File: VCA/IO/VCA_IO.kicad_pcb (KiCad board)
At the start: 2 copper layers, 29.5 x 111.8 mm, 15 parts, among them J1 Out_B, J10 IO_B, J11 Power, J2 CV1_B, J3 In_B, J4 CV2_B, J5 IO_A, J6 CV1_A, J7 In_A, J8 CV2_A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

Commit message: Clean up VCA boards
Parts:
- added REF**: OSHW-Logo2_7.3x6mm_SilkScreen, Symbol:OSHW-Logo2_7.3x6mm_SilkScreen, B.Cu at (69.8, 64.8)
- J10, J5: moved to B.Cu
- moved J10 0.63 mm to (91.4, 106.7), turned to 180 degrees
- turned J5 to 180 degrees
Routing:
- net Net-(J10-Pad2): track 17.6 -> 19.5 mm
- net Net-(J1-PadT): track 30.3 -> 31.5 mm
- net Net-(J10-Pad8): track 23.6 -> 24.5 mm
- net Net-(J10-Pad7): track 20.2 -> 20.8 mm
- net Net-(J10-Pad6): track 13.5 -> 14.2 mm
- net Net-(J10-Pad4): track 56.8 -> 57.5 mm
- net Net-(J10-Pad5): track 23.8 -> 24.4 mm
- net Net-(J10-Pad3): track 48.9 -> 49.5 mm
- net GNDREF: vias 6 -> 4
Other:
- board text added: "CV1"
- board text added: "CV1 A"
- board text added: "CV1 B"
- board text added: "CV2"
- board text added: "CV2 A"
- board text added: "CV2 B"
- board text added: "In"
- board text added: "In A"
- board text added: "In B"
- board text added: "Level"
- board text added: "Level A"
- board text added: "Level B"
- board text added: "Log/Lin A"
- board text added: "Log/Lin B"
- board text added: "Out"
- board text added: "Out A"
- board text added: "Out B"
- board text added: "Pwr"
- board text added: "SW_1"
- board text added: "SW_2"
- board text added: "SW_3"
- board text added: "VCA A IO"
- board text added: "VCA B IO"
- board text added: "VCO IO Board Rev 1"
- board text added: "WH"

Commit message: Bunch of bug fixes and tweaks
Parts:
- added H1: Top_MH1, Eurorack:eurorack_mounting_hole, F.Cu at (66.7, 78.7)
- added H2: Bottom_MH1, Eurorack:eurorack_mounting_hole, F.Cu at (66.7, 135.9)
- added H3: Top_MH2, Eurorack:eurorack_mounting_hole, F.Cu at (90.8, 78.7)
- added H4: Bottom_MH2, Eurorack:eurorack_mounting_hole, F.Cu at (90.8, 135.9)
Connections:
- RV1 pad : GNDREF -> (no net)
- RV2 pad : GNDREF -> (no net)
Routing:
- net GNDREF: vias 4 -> 0

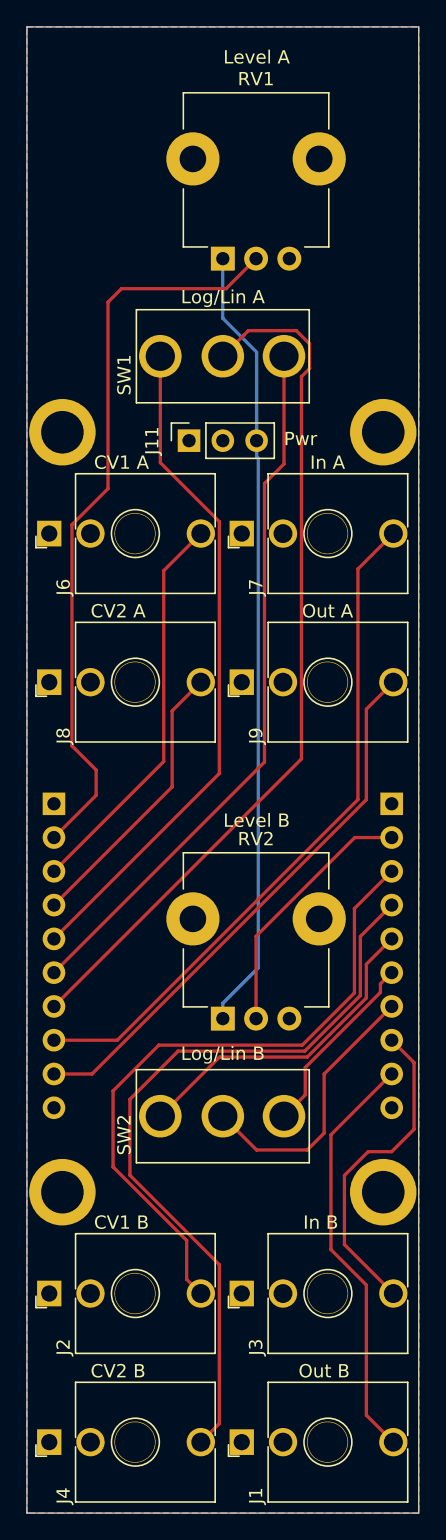
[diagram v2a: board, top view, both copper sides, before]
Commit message: Clean up layout of VCA board
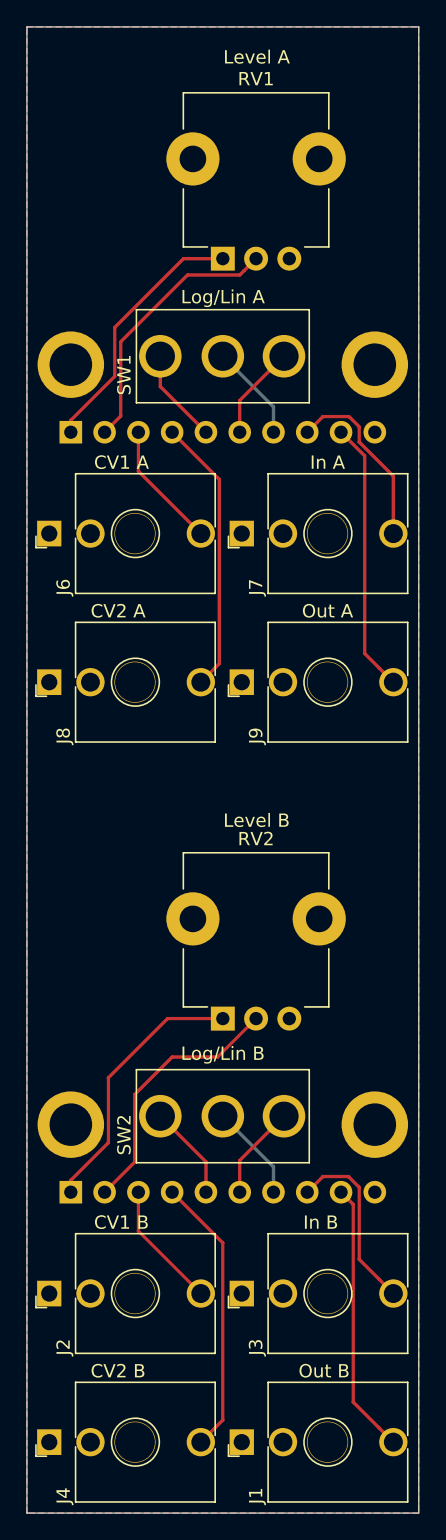
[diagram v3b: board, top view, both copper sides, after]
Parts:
- removed J11: Power, Connector_PinSocket_2.54mm:PinSocket_1x03_P2.54mm_Vertical
- removed REF**: OSHW-Logo2_7.3x6mm_SilkScreen, Symbol:OSHW-Logo2_7.3x6mm_SilkScreen
- moved J10 37.9 mm to (67.3, 135.9), turned to 270 degrees
- moved J5 28.0 mm to (67.3, 78.7), turned to 270 degrees
- moved H1 5.12 mm to (67.3, 73.7)
- moved H3 5.12 mm to (90.2, 73.7)
- moved H2 5.12 mm to (67.3, 130.8)
- moved H4 5.12 mm to (90.2, 130.8)
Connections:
- J10 pad 1: GNDREF -> +12VA
- J5 pad 1: GNDREF -> +12V
- RV1 pad : (no net) -> GNDREF
- RV1 pad 1: -12V -> +12V
- RV2 pad : (no net) -> GNDREF
- RV2 pad 1: -12V -> +12VA
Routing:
- net -12V: track 59.4 -> 0.00 mm
- net Net-(J5-Pad7): track 65.5 -> 7.29 mm
- net Net-(J5-Pad6): track 53.5 -> 7.09 mm
- net Net-(J5-Pad5): track 50.8 -> 7.14 mm
- net Net-(J10-Pad3): track 49.5 -> 9.57 mm
- net Net-(J5-Pad8): track 51.5 -> 13.8 mm
- net Net-(J10-Pad4): track 57.5 -> 21.1 mm
- net Net-(J5-Pad2): track 55.9 -> 20.1 mm
- net Net-(J5-Pad9): track 41.7 -> 20.4 mm
- net Net-(J5-Pad3): track 30.0 -> 9.57 mm
- net +12VA: track 0.00 -> 20.2 mm
- net +12V: track 0.00 -> 19.5 mm
- net Net-(J10-Pad5): track 24.4 -> 7.14 mm
- net Net-(J10-Pad7): track 20.8 -> 7.29 mm
- net Net-(J1-PadT): track 31.5 -> 20.4 mm
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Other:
- board text added: "+12V"
- board text added: "GND"
- board text removed: "Pwr"

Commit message: Added Gerber files
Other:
- board text added: "VCA IO Board Rev 1"
- board text removed: "VCO IO Board Rev 1"
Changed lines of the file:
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@@
       (drillshape 0)
       (scaleselection 1)
-      (outputdirectory ""))
+      (outputdirectory "Gerbers/"))
   )
   (net 0 "")
@@
     (effects (font (size 1 1) (thickness 0.15)) (justify mirror))
   )
-  (gr_text "VCO IO Board Rev 1" (at 85.09 49.53) (layer B.SilkS)
+  (gr_text "VCA IO Board Rev 1" (at 85.09 49.53) (layer B.SilkS)
     (effects (font (size 1 1) (thickness 0.15)) (justify mirror))
   )
@@
   (gr_line (start 93.472 48.26) (end 93.472 160.02) (layer Edge.Cuts) (width 0.05))
   (gr_line (start 64.008 48.26) (end 93.472 48.26) (layer Edge.Cuts) (width 0.05))
-  (segment (start 70.135001 132.166001) (end 70.135001 127.285001) (width 0.25) (layer F.Cu) (net 19))
-  (segment (start 67.31 134.991002) (end 70.135001 132.166001) (width 0.25) (layer F.Cu) (net 19))
-  (segment (start 67.31 135.89) (end 67.31 134.991002) (width 0.25) (layer F.Cu) (net 19) (status 10))
-  (segment (start 74.584002 122.836) (end 78.74 122.836) (width 0.25) (layer F.Cu) (net 19) (status 20))
-  (segment (start 70.135001 127.285001) (end 74.584002 122.836) (width 0.25) (layer F.Cu) (net 19))
   (segment (start 67.31 77.841002) (end 70.612 74.539002) (width 0.25) (layer F.Cu) (net 2))
   (segment (start 67.31 78.74) (end 67.31 77.841002) (width 0.25) (layer F.Cu) (net 2) (status 10))
@@
   (segment (start 78.346 125.73) (end 81.24 122.836) (width 0.25) (layer F.Cu) (net 18) (status 20))
   (segment (start 74.93 125.73) (end 78.346 125.73) (width 0.25) (layer F.Cu) (net 18))
+  (segment (start 70.135001 132.166001) (end 70.135001 127.285001) (width 0.25) (layer F.Cu) (net 19))
+  (segment (start 67.31 134.991002) (end 70.135001 132.166001) (width 0.25) (layer F.Cu) (net 19))
+  (segment (start 67.31 135.89) (end 67.31 134.991002) (width 0.25) (layer F.Cu) (net 19) (status 10))
+  (segment (start 74.584002 122.836) (end 78.74 122.836) (width 0.25) (layer F.Cu) (net 19) (status 20))
+  (segment (start 70.135001 127.285001) (end 74.584002 122.836) (width 0.25) (layer F.Cu) (net 19))
   (zone (net 1) (net_name GNDREF) (layer F.Cu) (hatch edge 0.508)
     (connect_pads (clearance 0.508))

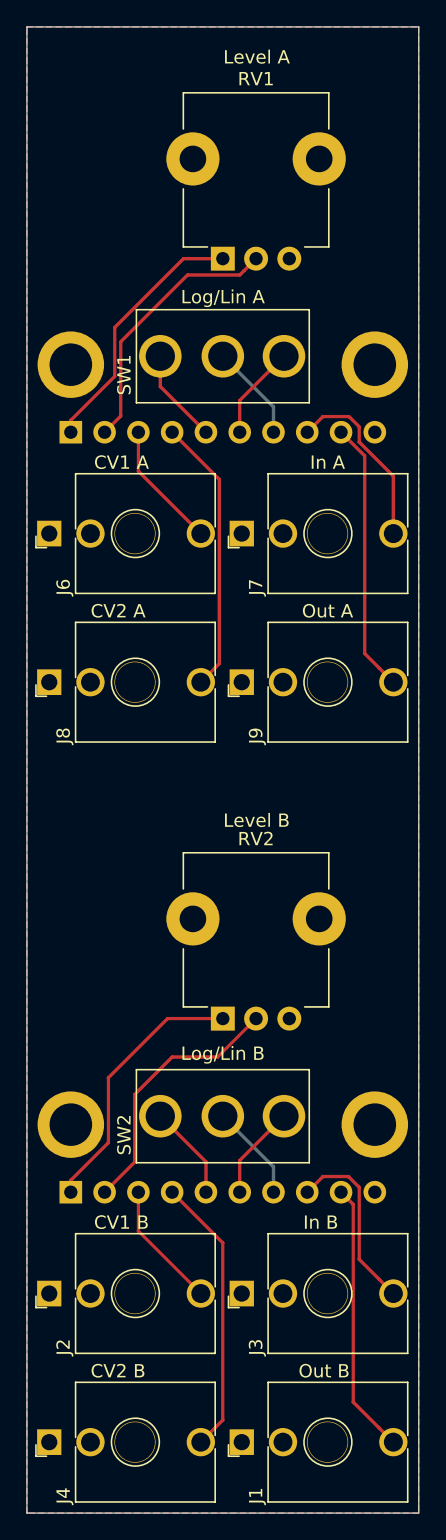
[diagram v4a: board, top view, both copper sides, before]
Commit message: Fix backwards knobs
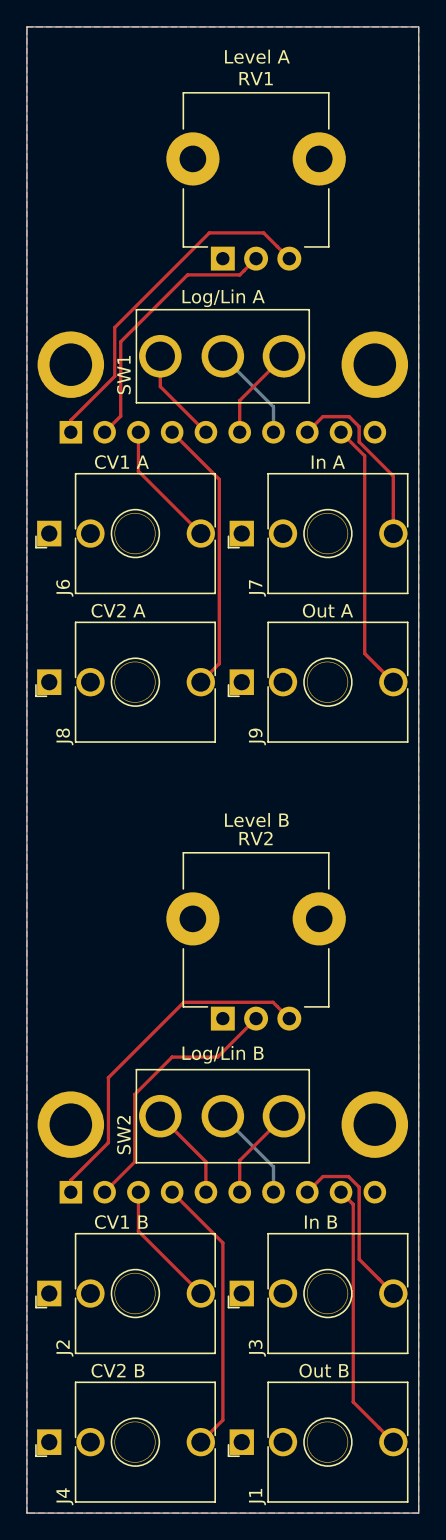
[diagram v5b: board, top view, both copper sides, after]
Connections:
- RV1 pad 1: +12V -> GNDREF
- RV1 pad 3: GNDREF -> +12V
- RV2 pad 1: +12VA -> GNDREF
- RV2 pad 3: GNDREF -> +12VA
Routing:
- net +12V: track 19.5 -> 26.1 mm
- net +12VA: track 20.2 -> 26.2 mm
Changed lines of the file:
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@@
     (thickness 1.6)
     (drawings 40)
-    (tracks 66)
+    (tracks 70)
     (zones 0)
     (modules 18)
@@
     (fp_line (start -5.64 -2.23) (end -5.64 -5.08) (layer F.CrtYd) (width 0.05))
     (pad 1 thru_hole rect (at -2.54 7.52) (size 1.8 1.8) (drill 1) (layers *.Cu *.Mask)
-      (net 2 +12V))
+      (net 1 GNDREF))
     (pad 2 thru_hole circle (at -0.04 7.52) (size 1.8 1.8) (drill 1) (layers *.Cu *.Mask)
       (net 7 "Net-(J5-Pad2)"))
     (pad 3 thru_hole circle (at 2.46 7.52) (size 1.8 1.8) (drill 1) (layers *.Cu *.Mask)
-      (net 1 GNDREF))
+      (net 2 +12V))
     (pad "" thru_hole oval (at -4.79 0.02) (size 4 4) (drill 2) (layers *.Cu *.Mask)
       (net 1 GNDREF))
@@
     (fp_line (start -5.64 -2.23) (end -5.64 -5.08) (layer F.CrtYd) (width 0.05))
     (pad 1 thru_hole rect (at -2.54 7.52) (size 1.8 1.8) (drill 1) (layers *.Cu *.Mask)
-      (net 19 +12VA))
+      (net 1 GNDREF))
     (pad 2 thru_hole circle (at -0.04 7.52) (size 1.8 1.8) (drill 1) (layers *.Cu *.Mask)
       (net 18 "Net-(J10-Pad2)"))
     (pad 3 thru_hole circle (at 2.46 7.52) (size 1.8 1.8) (drill 1) (layers *.Cu *.Mask)
-      (net 1 GNDREF))
+      (net 19 +12VA))
     (pad "" thru_hole oval (at -4.79 0.02) (size 4 4) (drill 2) (layers *.Cu *.Mask)
       (net 1 GNDREF))
@@
   (gr_line (start 93.472 48.26) (end 93.472 160.02) (layer Edge.Cuts) (width 0.05))
   (gr_line (start 64.008 48.26) (end 93.472 48.26) (layer Edge.Cuts) (width 0.05))
+  (segment (start 82.840001 64.786001) (end 83.74 65.686) (width 0.25) (layer F.Cu) (net 2))
+  (segment (start 67.31 78.74) (end 67.31 77.841002) (width 0.25) (layer F.Cu) (net 2))
+  (segment (start 70.612 70.866) (end 77.724 63.754) (width 0.25) (layer F.Cu) (net 2))
+  (segment (start 70.612 74.539002) (end 70.612 70.866) (width 0.25) (layer F.Cu) (net 2))
   (segment (start 67.31 77.841002) (end 70.612 74.539002) (width 0.25) (layer F.Cu) (net 2))
-  (segment (start 67.31 78.74) (end 67.31 77.841002) (width 0.25) (layer F.Cu) (net 2) (status 10))
-  (segment (start 70.612 74.539002) (end 70.612 70.866) (width 0.25) (layer F.Cu) (net 2))
-  (segment (start 75.792 65.686) (end 78.74 65.686) (width 0.25) (layer F.Cu) (net 2) (status 20))
-  (segment (start 70.612 70.866) (end 75.792 65.686) (width 0.25) (layer F.Cu) (net 2))
+  (segment (start 81.808 63.754) (end 82.840001 64.786001) (width 0.25) (layer F.Cu) (net 2))
+  (segment (start 77.724 63.754) (end 81.808 63.754) (width 0.25) (layer F.Cu) (net 2))
   (segment (start 90.499001 153.621001) (end 91.564 154.686) (width 0.25) (layer F.Cu) (net 3) (status 20))
   (segment (start 88.544989 151.666989) (end 90.499001 153.621001) (width 0.25) (layer F.Cu) (net 3))
@@
   (segment (start 78.346 125.73) (end 81.24 122.836) (width 0.25) (layer F.Cu) (net 18) (status 20))
   (segment (start 74.93 125.73) (end 78.346 125.73) (width 0.25) (layer F.Cu) (net 18))
+  (segment (start 82.514999 121.610999) (end 82.840001 121.936001) (width 0.25) (layer F.Cu) (net 19))
+  (segment (start 75.809003 121.610999) (end 82.514999 121.610999) (width 0.25) (layer F.Cu) (net 19))
   (segment (start 70.135001 132.166001) (end 70.135001 127.285001) (width 0.25) (layer F.Cu) (net 19))
+  (segment (start 70.135001 127.285001) (end 75.809003 121.610999) (width 0.25) (layer F.Cu) (net 19))
+  (segment (start 82.840001 121.936001) (end 83.74 122.836) (width 0.25) (layer F.Cu) (net 19))
   (segment (start 67.31 134.991002) (end 70.135001 132.166001) (width 0.25) (layer F.Cu) (net 19))
-  (segment (start 67.31 135.89) (end 67.31 134.991002) (width 0.25) (layer F.Cu) (net 19) (status 10))
-  (segment (start 74.584002 122.836) (end 78.74 122.836) (width 0.25) (layer F.Cu) (net 19) (status 20))
-  (segment (start 70.135001 127.285001) (end 74.584002 122.836) (width 0.25) (layer F.Cu) (net 19))
+  (segment (start 67.31 135.89) (end 67.31 134.991002) (width 0.25) (layer F.Cu) (net 19))
   (zone (net 1) (net_name GNDREF) (layer F.Cu) (hatch edge 0.508)
     (connect_pads (clearance 0.508))
